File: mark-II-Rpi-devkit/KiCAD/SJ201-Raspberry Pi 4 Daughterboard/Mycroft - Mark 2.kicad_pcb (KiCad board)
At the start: 4 copper layers, 72 x 93 mm, 210 parts, among them J1 Barrel_Jack, J10 Debug Connector, J2 PVDD Jumper, J3 SPKLEFT, J4 SPKRIGHT, J5 PowerTP, J6 Raspberry_Pi_4, J7 USB_B_Micro, J9 USB_A, P1 LED, P2 LED, P3 LED, P4 LED, Q3 AO3415A, Q4 FDV301N, SW1 MuteMic, U1 XL4015, U10 MP34DT05, U11 MP34DT05, U12 NCP303LSN30, U2 PCM2706, U3 MAX9744, U4 AZ1117CH-3.3, U5 74LVC125A, U6 FE1.1s, U7 AP3428A, U8 XMOS-XVF3510, U9 AT25SF161 16MBIT, X1 SG-210STF 24M, Y1 12MHz, Y2 12MHz

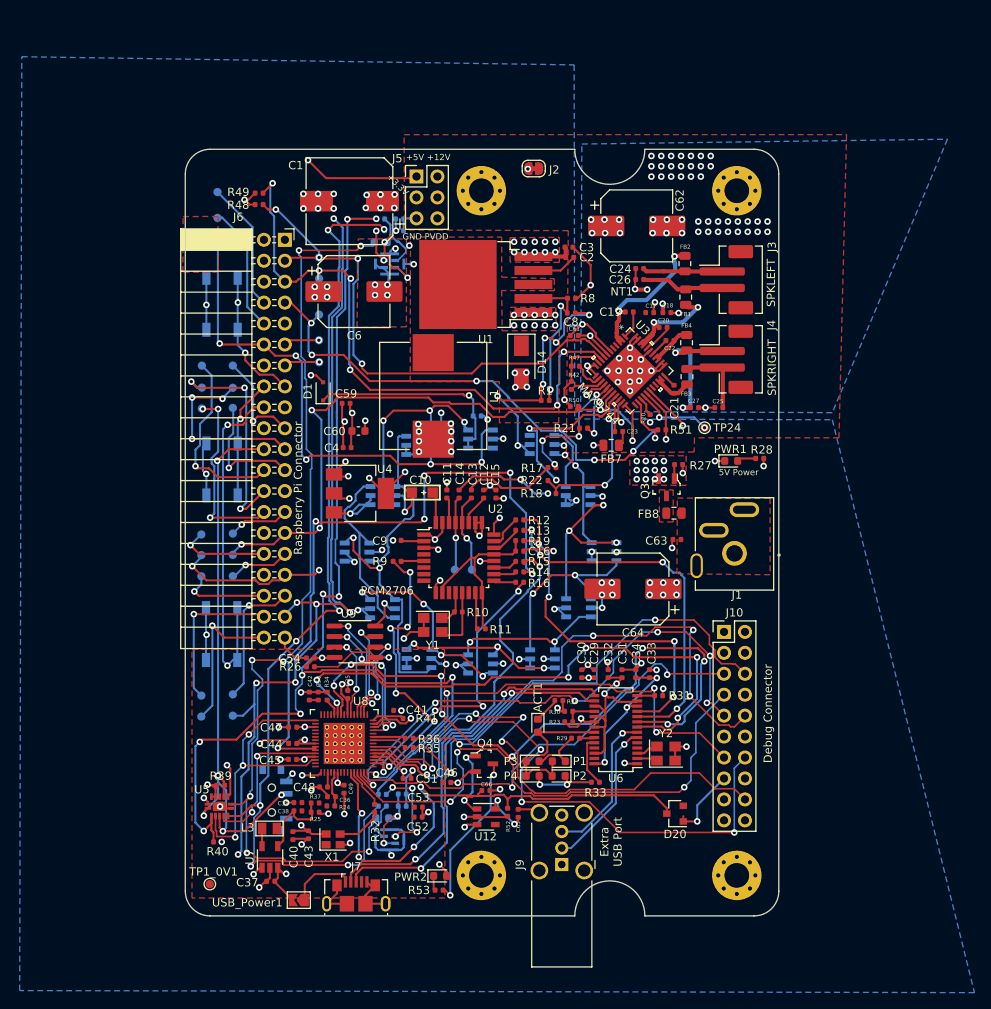
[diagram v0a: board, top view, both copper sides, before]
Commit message: Updated KiCAD files to 0.63 for PCB printing & Assembly at JLCPCB
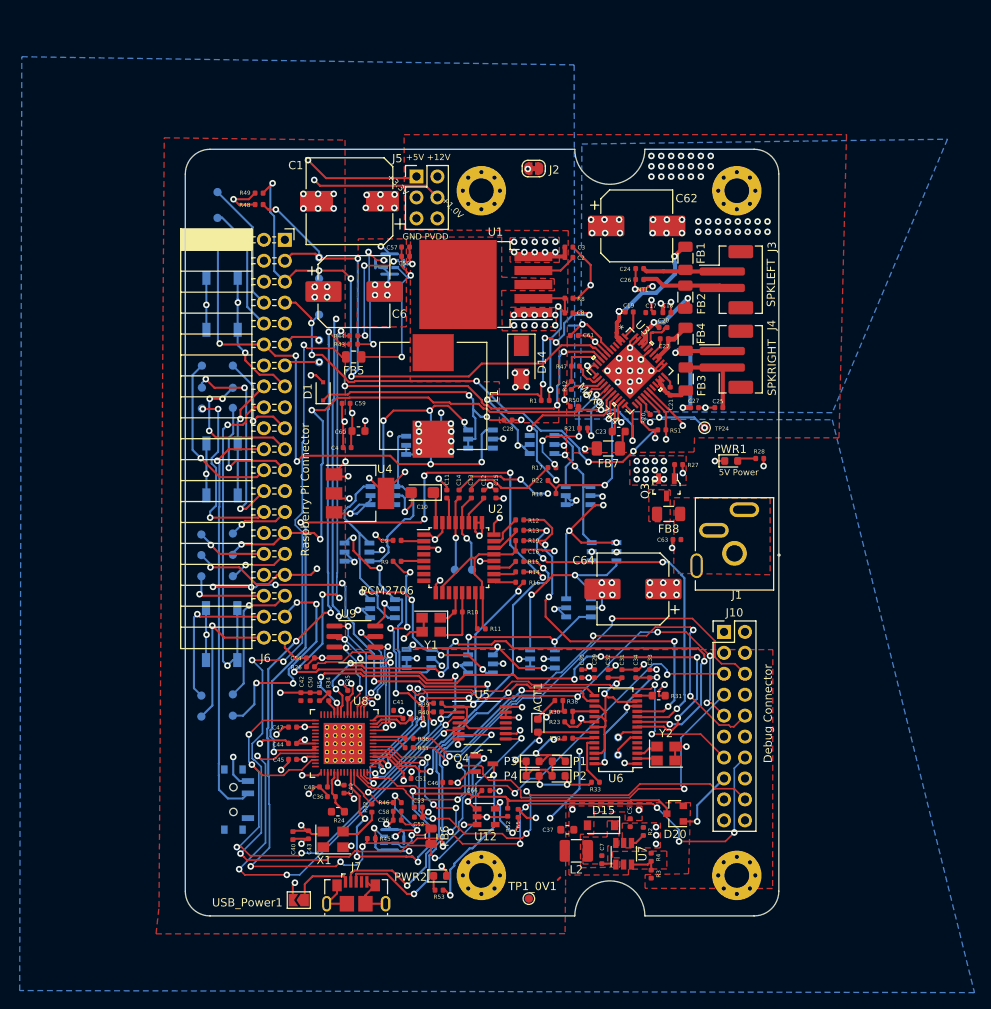
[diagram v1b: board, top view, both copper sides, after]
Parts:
- removed C38: 47pf, Capacitor_SMD:C_0402_1005Metric
- removed C39: 10UF, Capacitor_SMD:C_0402_1005Metric
- removed J9: USB_A, Connector_USB:USB_A_Wuerth_614004134726_Horizontal
- removed L3: 2.2UH-20%-1.2A_0805, OPL_Inductor:L0805
- removed R25: 47K, Resistor_SMD:R_0402_1005Metric
- removed R37: 30K, Resistor_SMD:R_0402_1005Metric
- added C5: 10UF, Capacitor_SMD:C_0402_1005Metric, F.Cu at (54.4, 86.6)
- added C7: 10nF, Capacitor_SMD:C_0402_1005Metric, F.Cu at (50.9, 91.1)
- added D15: D_Schottky, Diode_SMD:D_SOD-123, F.Cu at (50.8, 86.9)
- added DM3: TestPoint, TestPoint:TestPoint_Pad_D1.0mm, B.Cu at (52.9, 78.4)
- added DP3: TestPoint, TestPoint:TestPoint_Pad_D1.0mm, B.Cu at (52.9, 76.2)
- added L2: 2.2UH ±30% 1.55A, Inductor_SMD:L_1210_3225Metric, F.Cu at (47.8, 90.0)
- added R2: 100K, Resistor_SMD:R_0402_1005Metric, F.Cu at (56.0, 87.6)
- added R3: 75k, Resistor_SMD:R_0402_1005Metric, F.Cu at (56.9, 92.8)
- added R4: 330K, Resistor_SMD:R_0402_1005Metric, F.Cu at (56.9, 90.8)
- added R5: 10R, Resistor_SMD:R_0402_1005Metric, F.Cu at (16.7, 71.3)
- C10: footprint OPL_Capacitor:AVX-A(1206) -> Capacitor_Tantalum_SMD:CP_EIA-3216-18_Kemet-A
- C23: footprint Capacitor_SMD:C_0402_1005Metric -> Capacitor_SMD:C_0603_1608Metric
- C28, C55, C56, C57, C58, R43, R44, R45, R46: moved to F.Cu
- C37: value 10UF -> 22UF; footprint Capacitor_SMD:C_0402_1005Metric -> Capacitor_SMD:C_0603_1608Metric
- C6, C62, C64: footprint user:CP_Elec_8x10.5_OPL -> Capacitor_SMD:CP_Elec_8x10.5
- FB1, FB2, FB3, FB4, FB7, FB8: footprint Resistor_SMD:R_0805_2012Metric -> Resistor_SMD:R_1206_3216Metric
- FB5, FB6: footprint Resistor_SMD:R_0603_1608Metric -> Resistor_SMD:R_0805_2012Metric; moved to F.Cu
- R24, R31: footprint Resistor_SMD:R_0402_1005Metric -> Resistor_SMD:R_0603_1608Metric
- R34: value 43R2 -> 33R
- U1: value XL4015 -> XL4501E1
- U10, U11: value MP34DT05 -> SPK0838HT4H-1
- U5: value 74LVC125A -> SN74LVC125APWR; footprint mycroft:DHVQFN14 -> Package_SO:TSSOP-14_4.4x5mm_P0.65mm
- U7: value AP3428A -> MP2359; footprint Package_TO_SOT_SMD:TSOT-23-5 -> Package_TO_SOT_SMD:TSOT-23-6
- X1: footprint Oscillator:Oscillator_SMD_SeikoEpson_SG210-4Pin_2.5x2.0mm -> Oscillator:Oscillator_SMD_SeikoEpson_SG8002CE-4Pin_3.2x2.5mm
- moved U7 42.9 mm to (53.6, 90.3)
- moved TP1_0V1 38.7 mm to (42.1, 95.8)
- moved C37 36.5 mm to (46.7, 87.4)
- moved U5 33.4 mm to (36.4, 74.5)
- moved R40 31.0 mm to (31.0, 73.1), turned to 0 degrees
- moved R39 28.1 mm to (31.0, 72.1)
- moved R44 14.5 mm to (20.8, 27.5)
- moved FB5 14.3 mm to (20.8, 30.1)
- moved R43 14.2 mm to (20.8, 28.5), turned to 0 degrees
- moved FB6 6.30 mm to (30.2, 88.2), turned to 270 degrees
- moved SW1 4.65 mm to (6.57, 83.8)
- moved C55 4.59 mm to (27.1, 17.9)
- moved R45 4.16 mm to (23.0, 88.5)
- moved C28 3.78 mm to (39.6, 37.7)
- moved C56 3.22 mm to (26.1, 86.3), turned to 180 degrees
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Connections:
- C37 pad 1: GND -> +1V0
- C37 pad 2: +5V -> GND
- J5 pad 4: Net-(J5-Pad4) -> +1V0
- R34 pad 2: GND -> Net-(R34-Pad2)
- U7 pad 1: +5V -> Net-(C7-Pad2)
- U7 pad 3: +5V -> Net-(R3-Pad2)
- U7 pad 5: Net-(L3-Pad1) -> +5V
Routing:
- net Net-(J6-Pad37): track 99.7 -> 26.3 mm, vias 7 -> 4
- net /xmos/MIC_DATA_M: track 136.5 -> 94.0 mm, vias 9 -> 7
- net GND: track 215.7 -> 255.6 mm, vias 101 -> 104
- net GPIO25: track 72.9 -> 111.8 mm, vias 5 -> 8
- net /xmos/MIC_CLK: track 18.8 -> 57.2 mm, vias 2 -> 4
- net /xmos/MIC_DATA: track 35.8 -> 67.5 mm, vias 3 -> 5
- net +1V0: track 6.30 -> 31.2 mm, vias 1 -> 4
- net Net-(DP3-Pad1): track 18.2 -> 2.56 mm
- net Net-(DM3-Pad1): track 18.3 -> 3.58 mm
- net Net-(R43-Pad2): track 4.05 -> 15.7 mm, vias 2 -> 3
- net USB_XMOS_D_P: track 80.5 -> 70.3 mm, vias 8 -> 6
- net /xmos/3V3_MIC0: track 11.6 -> 21.6 mm, vias 3 -> 2
- net /xmos/3V3_MIC: track 113.5 -> 123.1 mm, vias 7 -> 6
- net Net-(R2-Pad2): track 10.2 -> 1.82 mm
- net Net-(R44-Pad2): track 7.53 -> 13.5 mm, vias 1 -> 3
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- added copper zone on F.Cu, net Net-(C7-Pad1)
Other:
- board text added: "+1.0V"
- board text added: "+12V +5V"
- board text added: "3.3V+"
- board text added: "5V 5V GND GP18 GND GP23 GP24 GND GP25 GND GND"
- board text added: "8-16V"
- board text added: "GND"
- board text added: "GND XL1 UP1 GND XL UP0 GND XL DN0 GND XL DN1 GND"
- board text added: "JLCJLCJLCJLC"
- board text added: "Mycroft MK2 v0.63 SJ201-01-01"
- board text added: "PVDD GND"
- board text added: "SDA SCL GP04 GND GP22 GND GP05 GND"
- board text added: "TDI TMS TCK TDO RST"
- board text removed: "Extra USB Port"
- board text removed: "Mycroft MK2 v0.60 SJ201-01-01"

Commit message: Change USB IC to CM108B, add in Line Out jack, prep for 2 PCB sandwich
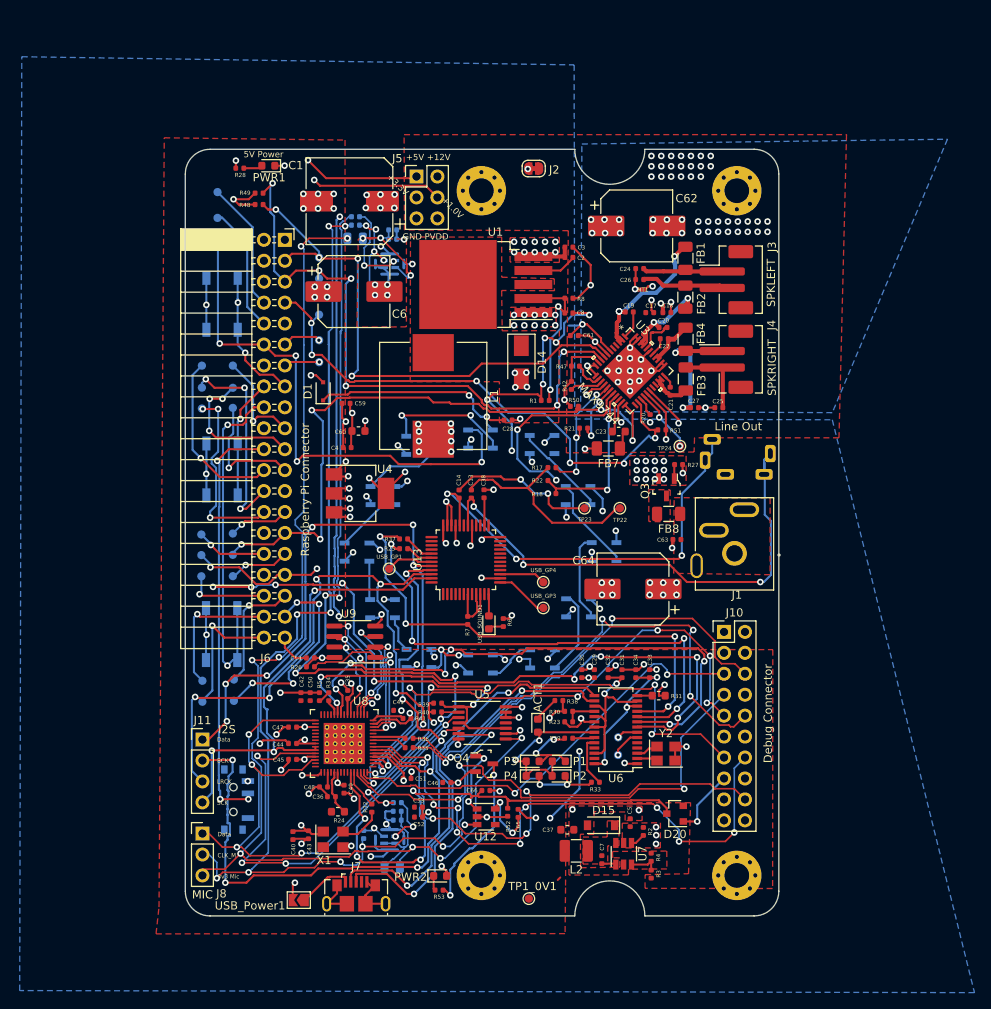
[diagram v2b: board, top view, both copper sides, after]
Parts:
- removed C10: 10UF, Capacitor_Tantalum_SMD:CP_EIA-3216-18_Kemet-A
- removed C11, C12, C15, C16, C9: 1uF, Capacitor_SMD:C_0402_1005Metric
- removed R10: 1M, Resistor_SMD:R_0402_1005Metric
- removed R11, R19: 1k5, Resistor_SMD:R_0402_1005Metric
- removed R12, R13, R14, R15, R16, R9: 22R, Resistor_SMD:R_0402_1005Metric
- removed U2: PCM2706, Package_QFP:TQFP-32_7x7mm_P0.8mm
- removed Y1: 12MHz, Crystal:Crystal_SMD_3225-4Pin_3.2x2.5mm
- added C38: 4.7UF, Capacitor_SMD:C_0402_1005Metric, F.Cu at (36.6, 46.7)
- added J11: I2S, Connector_PinHeader_2.54mm:PinHeader_1x04_P2.54mm_Vertical, F.Cu at (2.48, 76.5)
- added J8: MIC, Connector_PinHeader_2.54mm:PinHeader_1x03_P2.54mm_Vertical, F.Cu at (2.48, 87.9)
- added J9: AudioJack3_Ground_Switch, mycroft:STX-3790-5N, B.Cu at (67.0, 42.2)
- added R25: 22R, Resistor_SMD:R_0402_1005Metric, F.Cu at (26.9, 53.3)
- added R37: 22R, Resistor_SMD:R_0402_1005Metric, F.Cu at (26.9, 52.1)
- added R6: 330R, Resistor_SMD:R_0402_1005Metric, F.Cu at (39.0, 62.3)
- added R7: 1k5, Resistor_SMD:R_0402_1005Metric, F.Cu at (34.7, 62.0)
- added U13: CM108B, Package_QFP:LQFP-48_7x7mm_P0.5mm, F.Cu at (34.4, 54.7)
- added USB_GP1: TestPoint, TestPoint:TestPoint_Pad_D1.0mm, F.Cu at (25.1, 55.8)
- added USB_GP3: TestPoint, TestPoint:TestPoint_Pad_D1.0mm, F.Cu at (43.8, 60.5)
- added USB_GP4: TestPoint, TestPoint:TestPoint_Pad_D1.0mm, F.Cu at (43.8, 57.4)
- added USB_SOUND1: LED, LED_SMD:LED_0603_1608Metric, F.Cu at (37.2, 62.3)
- C55, C56, C57, C58, FB5, FB6, R43, R44, R45, R46: moved to B.Cu
- D10, D11, D12, D13, D2, D3, D4, D5, D6, D7, D8, D9: value WS2813 -> WS2812B; footprint user:LED_WS2813_3.5x3.5mm_P1.1mm -> user:LED_WS2812_Mini_3.5x3.5mm_P1.1mm
- TP22, TP23: moved to F.Cu
- moved R28 72.2 mm to (7.01, 7.17), turned to 180 degrees
- moved PWR1 66.6 mm to (10.5, 6.87), turned to 180 degrees
- moved TP22 19.4 mm to (53.1, 48.4)
- moved TP23 17.4 mm to (48.8, 48.4)
- moved R43 14.4 mm to (21.0, 14.1)
- moved R44 14.4 mm to (21.1, 13.1)
- moved FB5 14.4 mm to (21.0, 15.7)
- moved FB6 6.03 mm to (25.5, 92.0), turned to 0 degrees
- moved TP24 3.73 mm to (60.4, 40.9)
- moved C57 2.61 mm to (25.6, 14.7)
- moved C55 2.61 mm to (25.6, 15.8)
- moved TP20 1.80 mm to (2.48, 69.4)
- moved TP26 1.80 mm to (6.30, 71.8)
- moved TP19 1.80 mm to (6.30, 69.2)
- moved TP21 1.80 mm to (2.48, 71.9)
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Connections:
- D10 pad 2: +5V -> Net-(D10-Pad2)
- D10 pad 3: Net-(D10-Pad3) -> GND
- D11 pad 2: +5V -> Net-(D11-Pad2)
- D11 pad 3: Net-(D11-Pad3) -> GND
- D11 pad 4: Net-(D10-Pad3) -> Net-(D10-Pad2)
- D12 pad 2: +5V -> Net-(D12-Pad2)
- D12 pad 3: Net-(D12-Pad3) -> GND
- D12 pad 4: Net-(D11-Pad3) -> Net-(D11-Pad2)
- D13 pad 2: +5V -> Net-(D13-Pad2)
- D13 pad 3: Net-(D13-Pad3) -> GND
- D13 pad 4: Net-(D12-Pad3) -> Net-(D12-Pad2)
- D2 pad 2: Net-(C28-Pad1) -> Net-(D2-Pad2)
- D2 pad 3: Net-(D2-Pad3) -> GND
- D3 pad 2: +5V -> Net-(D3-Pad2)
- D3 pad 3: Net-(D3-Pad3) -> GND
- D3 pad 4: Net-(D2-Pad3) -> Net-(D2-Pad2)
- D4 pad 2: +5V -> Net-(D4-Pad2)
- D4 pad 3: Net-(D4-Pad3) -> GND
- D4 pad 4: Net-(D3-Pad3) -> Net-(D3-Pad2)
- D5 pad 2: +5V -> Net-(D5-Pad2)
- D5 pad 3: Net-(D5-Pad3) -> GND
- D5 pad 4: Net-(D4-Pad3) -> Net-(D4-Pad2)
- D6 pad 2: +5V -> Net-(D6-Pad2)
- D6 pad 3: Net-(D6-Pad3) -> GND
- D6 pad 4: Net-(D5-Pad3) -> Net-(D5-Pad2)
- D7 pad 2: +5V -> Net-(D7-Pad2)
- D7 pad 3: Net-(D7-Pad3) -> GND
- D7 pad 4: Net-(D6-Pad3) -> Net-(D6-Pad2)
- D8 pad 2: +5V -> Net-(D8-Pad2)
- D8 pad 3: Net-(D10-Pad6) -> GND
- D8 pad 4: Net-(D7-Pad3) -> Net-(D7-Pad2)
- D9 pad 2: +5V -> Net-(D10-Pad4)
- D9 pad 3: Net-(D10-Pad4) -> GND
- D9 pad 4: Net-(D10-Pad6) -> Net-(D8-Pad2)
- TP22 pad 1: VoutL -> Net-(C13-Pad2)
- TP23 pad 1: VoutR -> Net-(C14-Pad2)
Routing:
- net I2S_BCK: track 42.3 -> 98.3 mm, vias 2 -> 7
- net VoutL: track 9.46 -> 62.2 mm, vias 1 -> 3
- net I2S_DATA: track 35.5 -> 83.5 mm, vias 4 -> 7
- net I2S_LRCK: track 34.7 -> 81.4 mm, vias 6 -> 7
- net VoutR: track 8.93 -> 52.5 mm, vias 1 -> 3
- net Net-(D2-Pad3): track 27.0 -> 0.00 mm, vias 3 -> 0
- net I2S_SCK: track 83.8 -> 58.0 mm, vias 6 -> 3
- net /xmos/MIC_CLK_M: track 122.4 -> 148.2 mm, vias 8 -> 10
- net Net-(D5-Pad3): track 25.6 -> 0.00 mm, vias 2 -> 0
- net Net-(D6-Pad3): track 23.8 -> 0.00 mm, vias 4 -> 0
- net Net-(D4-Pad3): track 22.5 -> 0.00 mm
- net VDD: track 21.9 -> 0.00 mm
- net Net-(D10-Pad3): track 21.7 -> 0.00 mm, vias 3 -> 0
- net Net-(D3-Pad3): track 21.0 -> 0.00 mm
- net Net-(D7-Pad3): track 20.8 -> 0.00 mm, vias 3 -> 0
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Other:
- board text added: "Data BCK LRCK SCK"
- board text added: "Data CLK_M 3v3 Mic"
- board text added: "Line Out"
- board text added: "Mycroft MK2 v0.64 SJ201-01-01"
- board text removed: "Mycroft MK2 v0.63 SJ201-01-01"

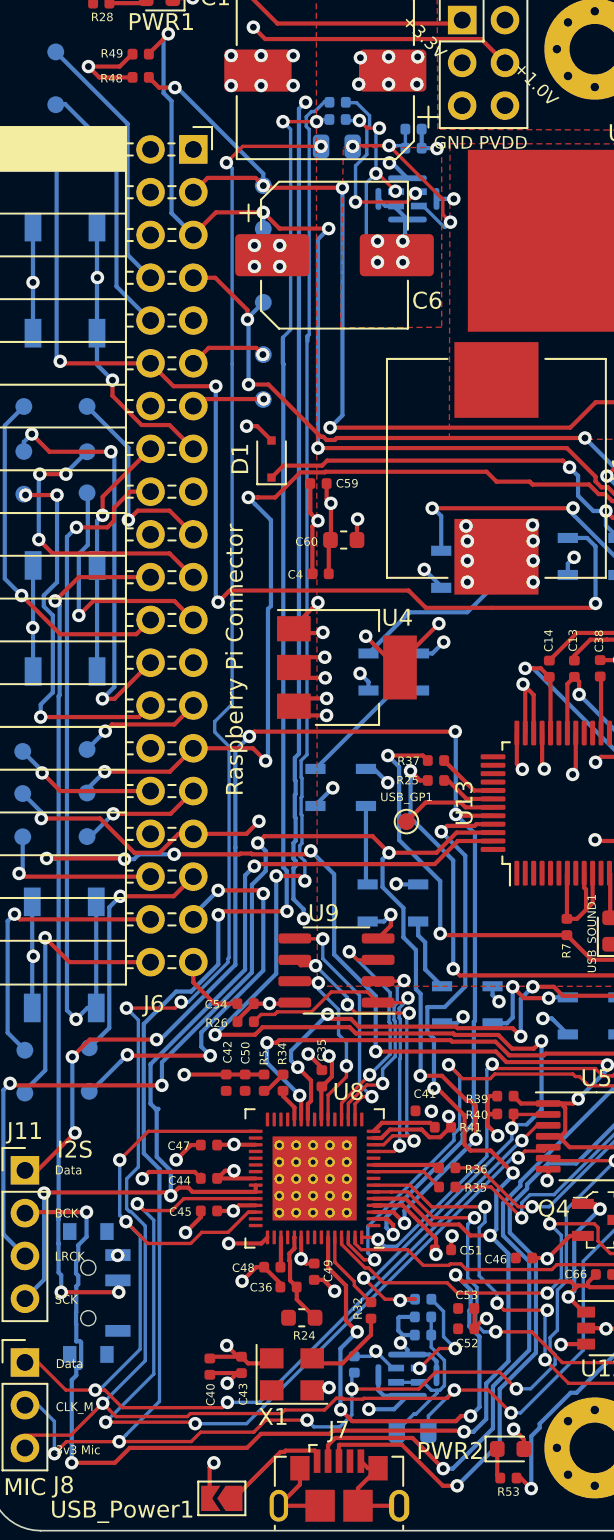
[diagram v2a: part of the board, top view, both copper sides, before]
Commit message: Change USB IC to CM108B, add in Line Out jack, prep for 2 PCB sandwich
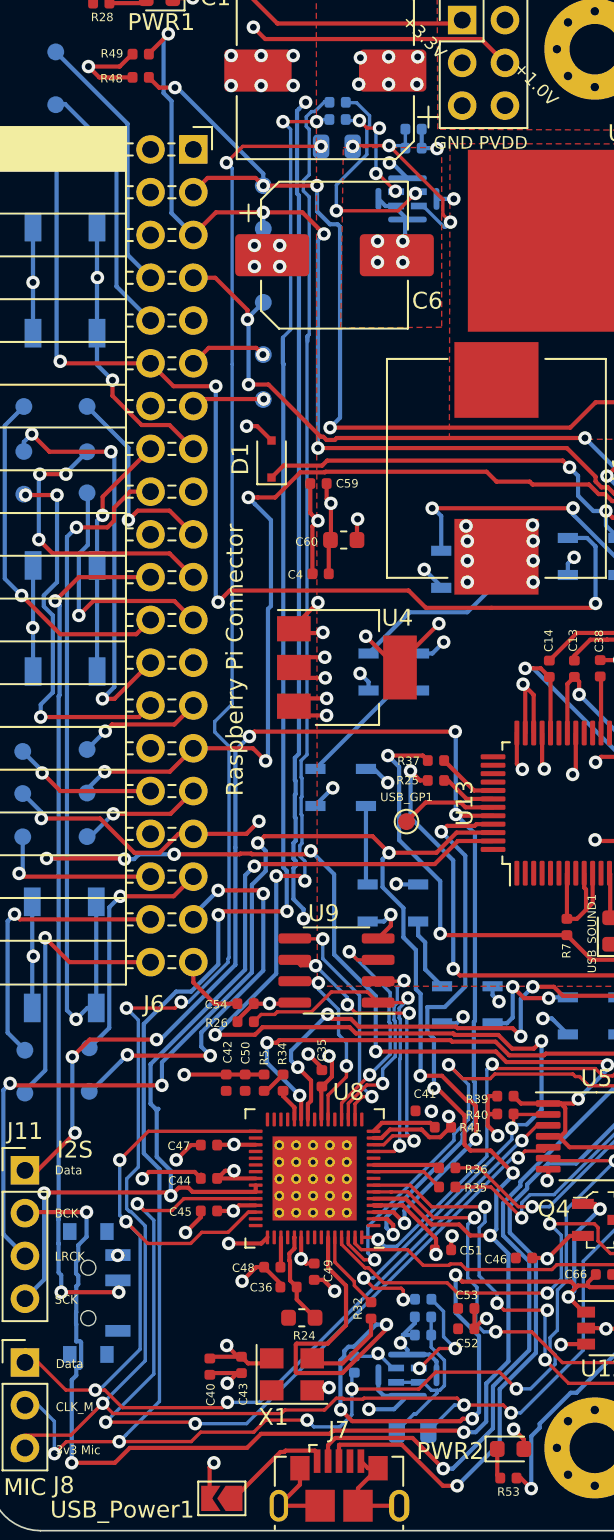
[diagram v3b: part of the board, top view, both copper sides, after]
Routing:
- net RST_N: track 72.5 -> 85.4 mm
- net Net-(R43-Pad2): track 12.5 -> 6.63 mm
- net Net-(R44-Pad2): track 11.3 -> 13.6 mm
- net /xmos/MIC_DATA_M: track 109.0 -> 107.8 mm
- net /xmos/3V3_MIC: track 142.9 -> 142.0 mm
- net GND: track 239.5 -> 238.9 mm
- net SDA_PI: track 66.7 -> 66.0 mm
- net SCL_PI: track 76.8 -> 76.2 mm
